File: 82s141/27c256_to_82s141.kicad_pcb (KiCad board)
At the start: 2 copper layers, 17.8 x 40.5 mm, 4 parts, among them J1 Conn_02x12_Counter_Clockwise, U1 27C256, U2 74LS02

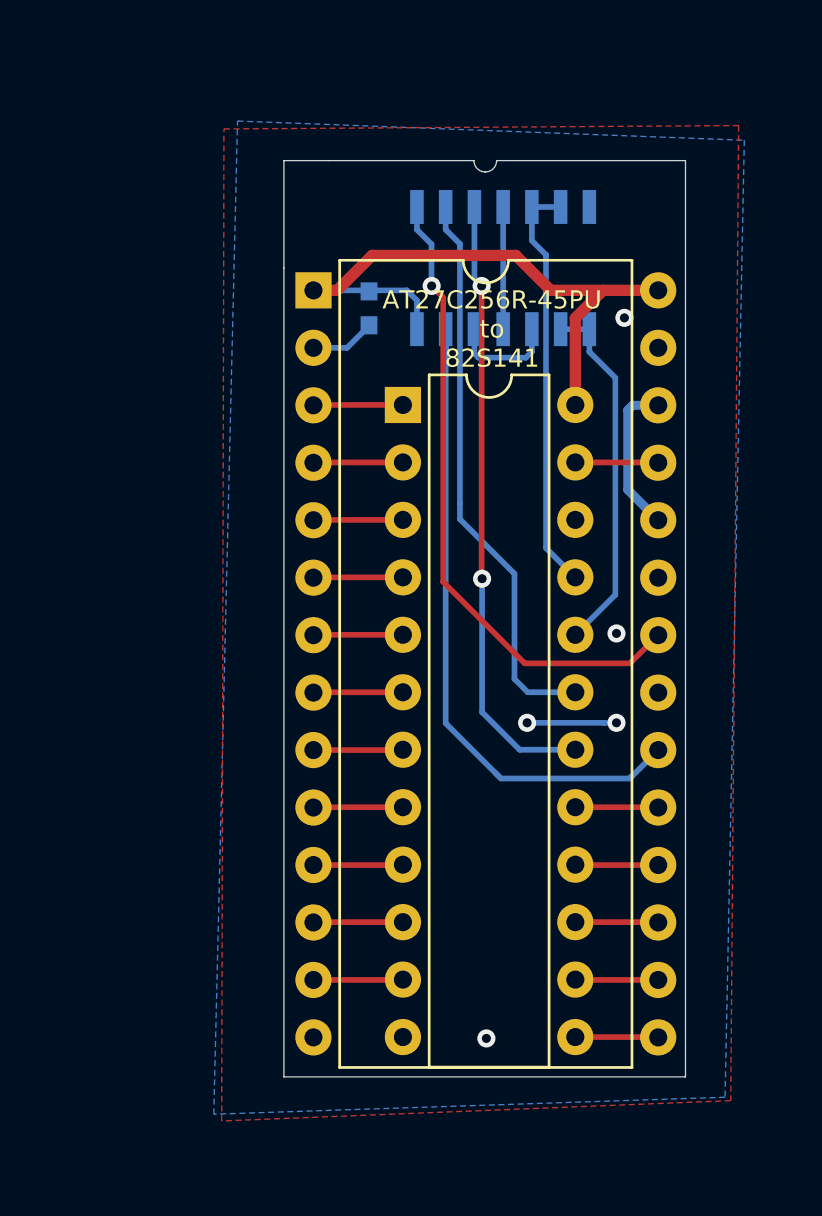
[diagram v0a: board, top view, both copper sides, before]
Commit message: Added 82S147 and redid 82S141
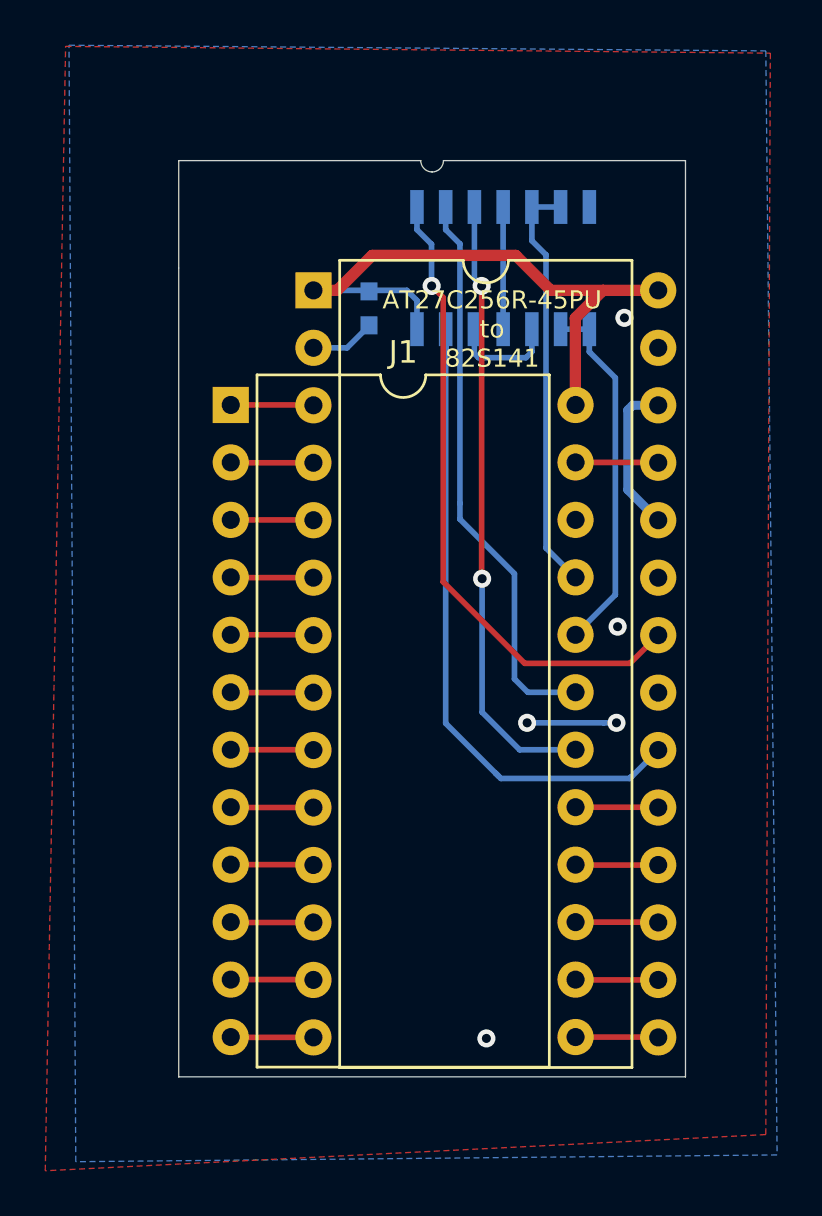
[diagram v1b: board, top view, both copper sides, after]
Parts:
- J1: footprint Housings_DIP:DIP-24_W7.62mm -> Housings_DIP:DIP-24_W15.24mm
- moved J1 7.61 mm to (107.2, 55.8)
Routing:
- net GND: track 13.7 -> 17.3 mm
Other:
- board size 17.8 x 40.5 mm -> 22.4 x 40.5 mm
